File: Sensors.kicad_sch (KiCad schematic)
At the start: 10 parts, among them U11 LSM6DSO32, U12 LIS2MDL, U13 MS5611-01BA

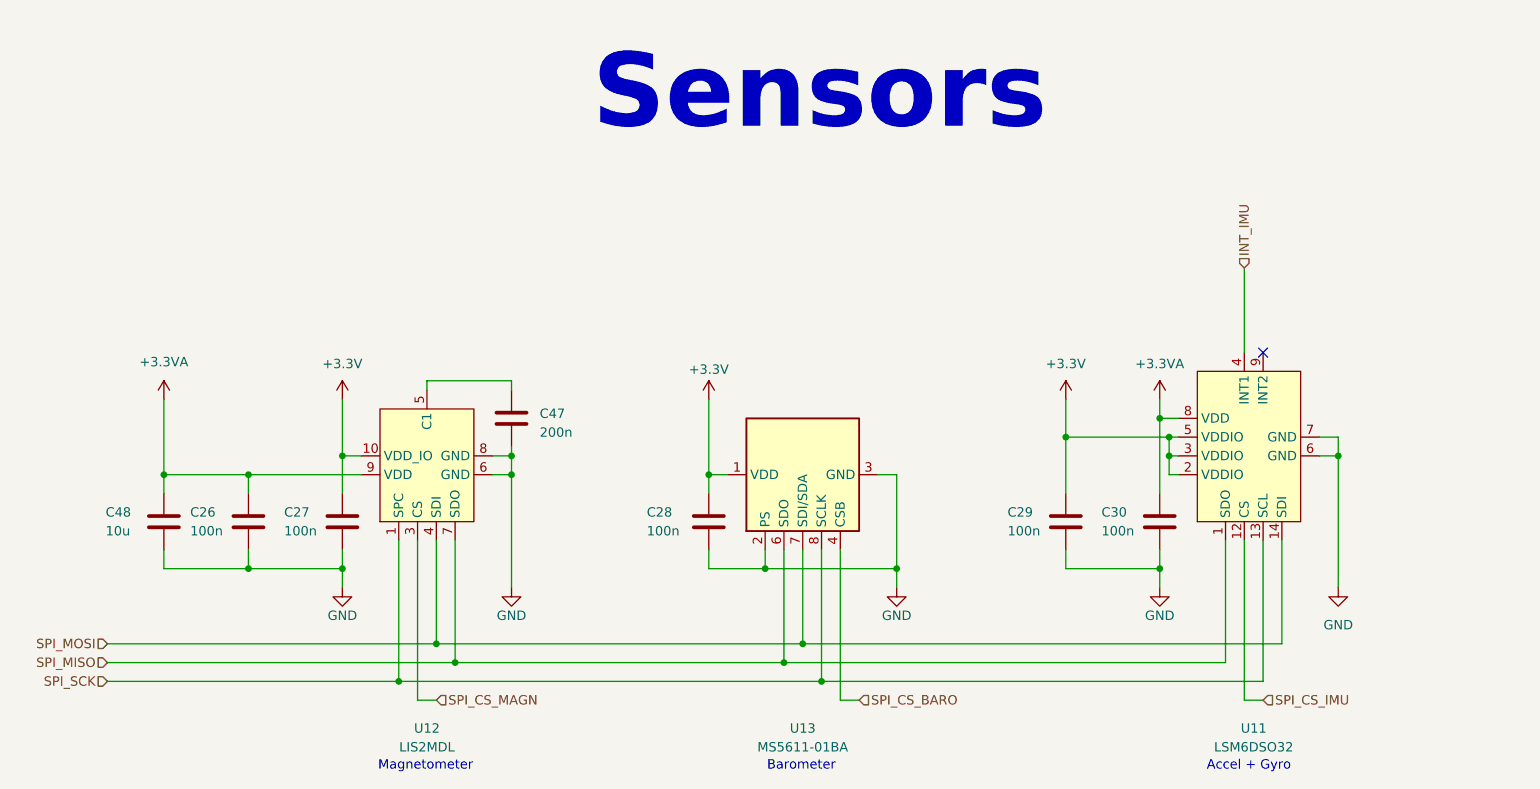
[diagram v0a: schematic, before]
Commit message: :building_construction: Simplify power circuit and consolidate BOM
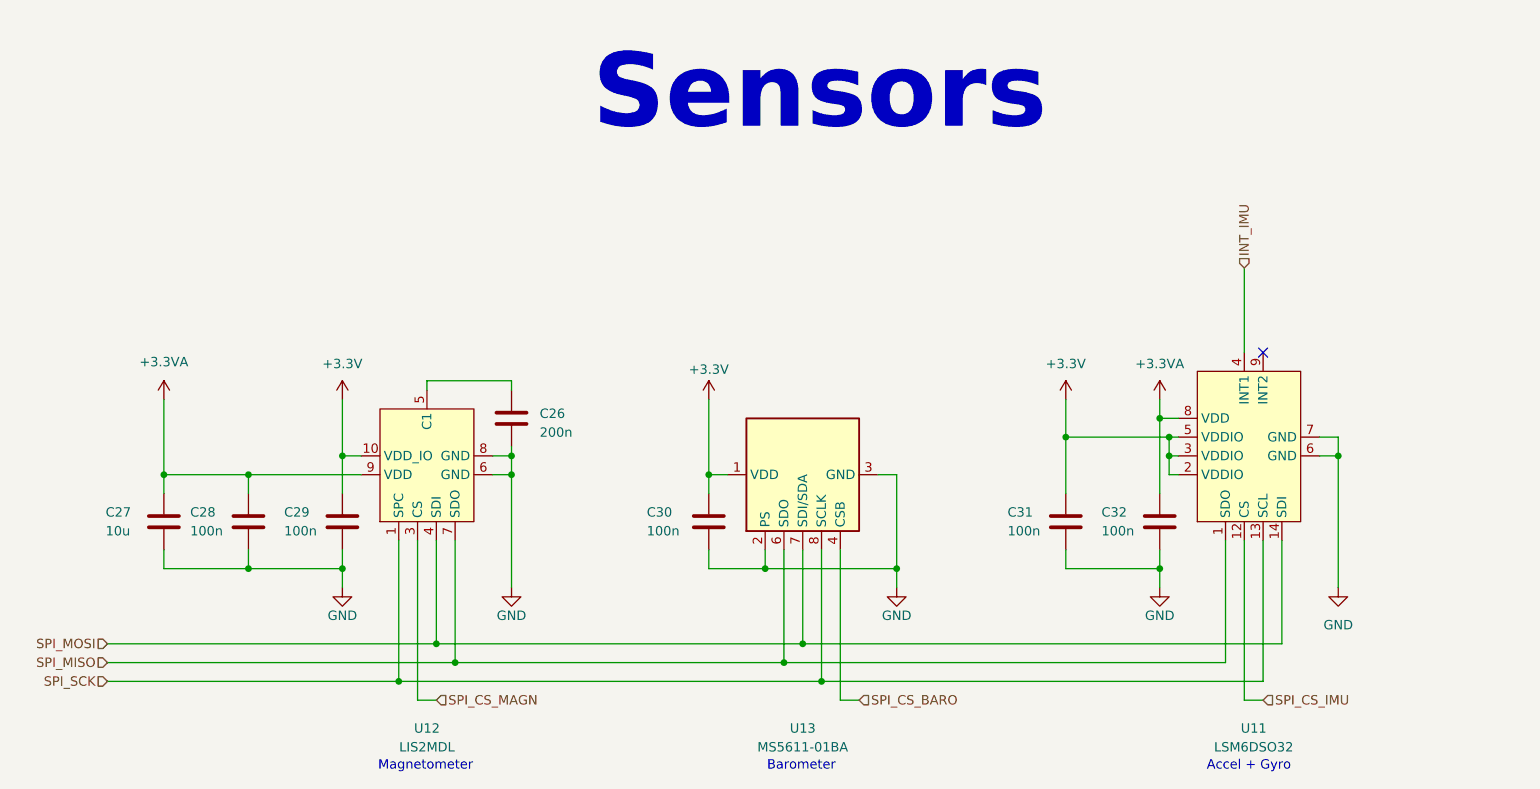
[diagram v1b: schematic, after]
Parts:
- renumbered C47 to C26, C48 to C27, C26 to C28, C27 to C29, C28 to C30, C29 to C31, C30 to C32
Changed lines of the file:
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@@
   (symbol (lib_id "Device:C") (at 58.42 102.87 0) (unit 1)
     (in_bom yes) (on_board yes) (dnp no)
-    (property "Reference" "C48" (at 50.546 101.6 0)
+    (property "Reference" "C27" (at 50.546 101.6 0)
       (effects (font (size 1.27 1.27)) (justify left))
     )
@@
   (symbol (lib_id "power:GND") (at 105.41 111.76 0) (unit 1)
     (in_bom yes) (on_board yes) (dnp no)
-    (property "Reference" "#PWR051" (at 105.41 118.11 0)
+    (property "Reference" "#PWR052" (at 105.41 118.11 0)
       (effects (font (size 1.27 1.27)) hide)
     )
@@
       (project "Nova"
         (path "/0c006d9f-ae30-49aa-ab15-ff0bec4de0e8/b4564e06-ae37-4733-9020-dc4bb7ce2d2c"
-          (reference "#PWR051") (unit 1)
+          (reference "#PWR052") (unit 1)
         )
       )
@@
   (symbol (lib_id "power:GND") (at 193.04 111.76 0) (unit 1)
     (in_bom yes) (on_board yes) (dnp no)
-    (property "Reference" "#PWR053" (at 193.04 118.11 0)
+    (property "Reference" "#PWR054" (at 193.04 118.11 0)
       (effects (font (size 1.27 1.27)) hide)
     )
@@
       (project "Nova"
         (path "/0c006d9f-ae30-49aa-ab15-ff0bec4de0e8/b4564e06-ae37-4733-9020-dc4bb7ce2d2c"
-          (reference "#PWR053") (unit 1)
+          (reference "#PWR054") (unit 1)
         )
       )
@@
   (symbol (lib_id "Device:C") (at 193.04 102.87 0) (unit 1)
     (in_bom yes) (on_board yes) (dnp no)
-    (property "Reference" "C30" (at 185.166 101.6 0)
+    (property "Reference" "C32" (at 185.166 101.6 0)
       (effects (font (size 1.27 1.27)) (justify left))
     )
@@
   (symbol (lib_id "Device:C") (at 105.41 88.9 0) (unit 1)
     (in_bom yes) (on_board yes) (dnp no) (fields_autoplaced)
-    (property "Reference" "C47" (at 109.22 88.265 0)
+    (property "Reference" "C26" (at 109.22 88.265 0)
       (effects (font (size 1.27 1.27)) (justify left))
     )
@@
   (symbol (lib_id "power:+3.3VA") (at 193.04 86.36 0) (unit 1)
     (in_bom yes) (on_board yes) (dnp no)
-    (property "Reference" "#PWR049" (at 193.04 90.17 0)
+    (property "Reference" "#PWR050" (at 193.04 90.17 0)
       (effects (font (size 1.27 1.27)) hide)
     )
@@
       (project "Nova"
         (path "/0c006d9f-ae30-49aa-ab15-ff0bec4de0e8/b4564e06-ae37-4733-9020-dc4bb7ce2d2c"
-          (reference "#PWR049") (unit 1)
+          (reference "#PWR050") (unit 1)
         )
       )
@@
   (symbol (lib_id "Device:C") (at 69.85 102.87 0) (unit 1)
     (in_bom yes) (on_board yes) (dnp no)
-    (property "Reference" "C26" (at 61.976 101.6 0)
+    (property "Reference" "C28" (at 61.976 101.6 0)
       (effects (font (size 1.27 1.27)) (justify left))
     )
@@
   (symbol (lib_id "Device:C") (at 82.55 102.87 0) (unit 1)
     (in_bom yes) (on_board yes) (dnp no)
-    (property "Reference" "C27" (at 74.676 101.6 0)
+    (property "Reference" "C29" (at 74.676 101.6 0)
       (effects (font (size 1.27 1.27)) (justify left))
     )
@@
   (symbol (lib_id "Device:C") (at 180.34 102.87 0) (unit 1)
     (in_bom yes) (on_board yes) (dnp no)
-    (property "Reference" "C29" (at 172.466 101.6 0)
+    (property "Reference" "C31" (at 172.466 101.6 0)
       (effects (font (size 1.27 1.27)) (justify left))
     )
@@
   (symbol (lib_id "Device:C") (at 132.08 102.87 0) (unit 1)
     (in_bom yes) (on_board yes) (dnp no)
-    (property "Reference" "C28" (at 123.698 101.6 0)
+    (property "Reference" "C30" (at 123.698 101.6 0)
       (effects (font (size 1.27 1.27)) (justify left))
     )
@@
   (symbol (lib_id "power:+3.3V") (at 82.55 86.36 0) (unit 1)
     (in_bom yes) (on_board yes) (dnp no) (fields_autoplaced)
-    (property "Reference" "#PWR045" (at 82.55 90.17 0)
+    (property "Reference" "#PWR047" (at 82.55 90.17 0)
       (effects (font (size 1.27 1.27)) hide)
     )
@@
       (project "Nova"
         (path "/0c006d9f-ae30-49aa-ab15-ff0bec4de0e8/b4564e06-ae37-4733-9020-dc4bb7ce2d2c"
-          (reference "#PWR046") (unit 1)
+          (reference "#PWR047") (unit 1)
         )
       )
@@
   (symbol (lib_id "power:+3.3V") (at 180.34 86.36 0) (unit 1)
     (in_bom yes) (on_board yes) (dnp no) (fields_autoplaced)
-    (property "Reference" "#PWR048" (at 180.34 90.17 0)
+    (property "Reference" "#PWR049" (at 180.34 90.17 0)
       (effects (font (size 1.27 1.27)) hide)
     )
@@
       (project "Nova"
         (path "/0c006d9f-ae30-49aa-ab15-ff0bec4de0e8/b4564e06-ae37-4733-9020-dc4bb7ce2d2c"
-          (reference "#PWR048") (unit 1)
+          (reference "#PWR049") (unit 1)
         )
       )
@@
   (symbol (lib_id "power:GND") (at 157.48 111.76 0) (unit 1)
     (in_bom yes) (on_board yes) (dnp no)
-    (property "Reference" "#PWR052" (at 157.48 118.11 0)
+    (property "Reference" "#PWR053" (at 157.48 118.11 0)
       (effects (font (size 1.27 1.27)) hide)
     )
@@
       (project "Nova"
         (path "/0c006d9f-ae30-49aa-ab15-ff0bec4de0e8/b4564e06-ae37-4733-9020-dc4bb7ce2d2c"
-          (reference "#PWR052") (unit 1)
+          (reference "#PWR053") (unit 1)
         )
       )
@@
   (symbol (lib_id "power:GND") (at 217.17 111.76 0) (unit 1)
     (in_bom yes) (on_board yes) (dnp no) (fields_autoplaced)
-    (property "Reference" "#PWR054" (at 217.17 118.11 0)
+    (property "Reference" "#PWR055" (at 217.17 118.11 0)
       (effects (font (size 1.27 1.27)) hide)
     )
@@
       (project "Nova"
         (path "/0c006d9f-ae30-49aa-ab15-ff0bec4de0e8/b4564e06-ae37-4733-9020-dc4bb7ce2d2c"
-          (reference "#PWR054") (unit 1)
+          (reference "#PWR055") (unit 1)
         )
       )
@@
   (symbol (lib_id "power:+3.3V") (at 132.08 86.36 0) (unit 1)
     (in_bom yes) (on_board yes) (dnp no)
-    (property "Reference" "#PWR047" (at 132.08 90.17 0)
+    (property "Reference" "#PWR048" (at 132.08 90.17 0)
       (effects (font (size 1.27 1.27)) hide)
     )
@@
       (project "Nova"
         (path "/0c006d9f-ae30-49aa-ab15-ff0bec4de0e8/b4564e06-ae37-4733-9020-dc4bb7ce2d2c"
-          (reference "#PWR047") (unit 1)
+          (reference "#PWR048") (unit 1)
         )
       )
@@
   (symbol (lib_id "power:GND") (at 82.55 111.76 0) (unit 1)
     (in_bom yes) (on_board yes) (dnp no)
-    (property "Reference" "#PWR050" (at 82.55 118.11 0)
+    (property "Reference" "#PWR051" (at 82.55 118.11 0)
       (effects (font (size 1.27 1.27)) hide)
     )
@@
       (project "Nova"
         (path "/0c006d9f-ae30-49aa-ab15-ff0bec4de0e8/b4564e06-ae37-4733-9020-dc4bb7ce2d2c"
-          (reference "#PWR050") (unit 1)
+          (reference "#PWR051") (unit 1)
         )
       )
@@
       (project "Nova"
         (path "/0c006d9f-ae30-49aa-ab15-ff0bec4de0e8/b4564e06-ae37-4733-9020-dc4bb7ce2d2c"
-          (reference "#PWR045") (unit 1)
-        )
-      )
+          (reference "#PWR046") (unit 1)
+        )
+      )

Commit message: :building_construction: Replace debug header with TagConnect and inline STM32 decoupling caps
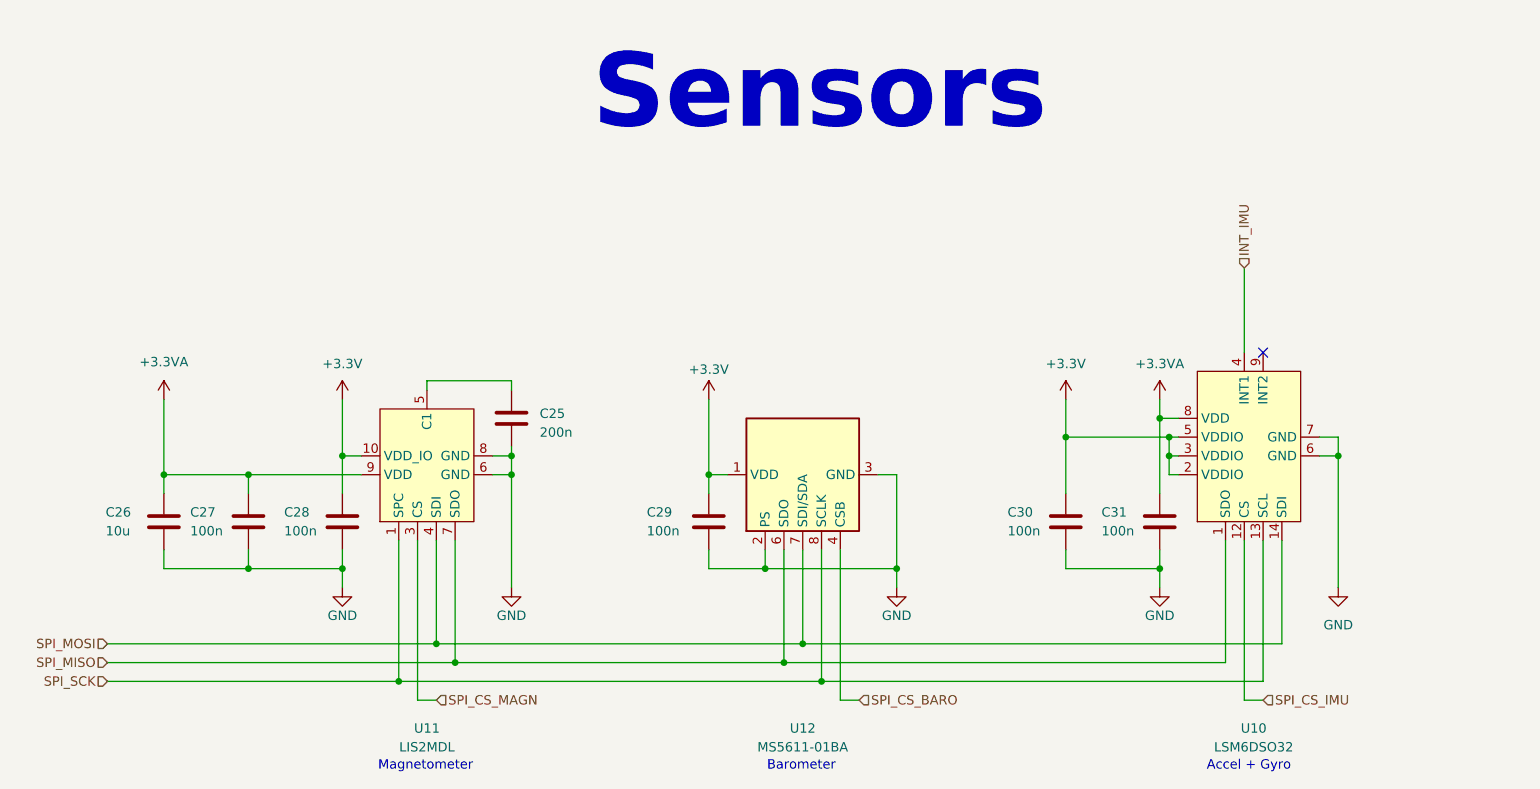
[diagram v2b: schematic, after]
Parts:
- renumbered C26 to C25, C27 to C26, C28 to C27, C29 to C28, C30 to C29, C31 to C30, C32 to C31, U11 to U10, U12 to U11, U13 to U12
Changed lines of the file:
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@@
   (symbol (lib_id "Device:C") (at 58.42 102.87 0) (unit 1)
     (in_bom yes) (on_board yes) (dnp no)
-    (property "Reference" "C27" (at 50.546 101.6 0)
+    (property "Reference" "C26" (at 50.546 101.6 0)
       (effects (font (size 1.27 1.27)) (justify left))
     )
@@
       (project "Nova"
         (path "/0c006d9f-ae30-49aa-ab15-ff0bec4de0e8/b4564e06-ae37-4733-9020-dc4bb7ce2d2c"
-          (reference "C27") (unit 1)
+          (reference "C26") (unit 1)
         )
       )
@@
   (symbol (lib_id "Odyssey:LIS2MDL") (at 87.63 95.25 90) (unit 1)
     (in_bom yes) (on_board yes) (dnp no)
-    (property "Reference" "U12" (at 93.98 130.81 90)
+    (property "Reference" "U11" (at 93.98 130.81 90)
       (effects (font (size 1.27 1.27)))
     )
@@
       (project "Nova"
         (path "/0c006d9f-ae30-49aa-ab15-ff0bec4de0e8/b4564e06-ae37-4733-9020-dc4bb7ce2d2c"
-          (reference "U12") (unit 1)
+          (reference "U11") (unit 1)
         )
       )
@@
   (symbol (lib_id "Device:C") (at 193.04 102.87 0) (unit 1)
     (in_bom yes) (on_board yes) (dnp no)
-    (property "Reference" "C32" (at 185.166 101.6 0)
+    (property "Reference" "C31" (at 185.166 101.6 0)
       (effects (font (size 1.27 1.27)) (justify left))
     )
@@
       (project "Nova"
         (path "/0c006d9f-ae30-49aa-ab15-ff0bec4de0e8/b4564e06-ae37-4733-9020-dc4bb7ce2d2c"
-          (reference "C32") (unit 1)
+          (reference "C31") (unit 1)
         )
       )
@@
   (symbol (lib_id "Device:C") (at 105.41 88.9 0) (unit 1)
     (in_bom yes) (on_board yes) (dnp no) (fields_autoplaced)
-    (property "Reference" "C26" (at 109.22 88.265 0)
+    (property "Reference" "C25" (at 109.22 88.265 0)
       (effects (font (size 1.27 1.27)) (justify left))
     )
@@
       (project "Nova"
         (path "/0c006d9f-ae30-49aa-ab15-ff0bec4de0e8/b4564e06-ae37-4733-9020-dc4bb7ce2d2c"
-          (reference "C26") (unit 1)
+          (reference "C25") (unit 1)
         )
       )
@@
   (symbol (lib_id "Device:C") (at 69.85 102.87 0) (unit 1)
     (in_bom yes) (on_board yes) (dnp no)
-    (property "Reference" "C28" (at 61.976 101.6 0)
+    (property "Reference" "C27" (at 61.976 101.6 0)
       (effects (font (size 1.27 1.27)) (justify left))
     )
@@
       (project "Nova"
         (path "/0c006d9f-ae30-49aa-ab15-ff0bec4de0e8/b4564e06-ae37-4733-9020-dc4bb7ce2d2c"
+          (reference "C27") (unit 1)
+        )
+      )
+    )
+  )
+  (symbol (lib_id "Device:C") (at 82.55 102.87 0) (unit 1)
+    (in_bom yes) (on_board yes) (dnp no)
+    (property "Reference" "C28" (at 74.676 101.6 0)
+      (effects (font (size 1.27 1.27)) (justify left))
+    )
+    (property "Value" "100n" (at 74.676 104.14 0)
+      (effects (font (size 1.27 1.27)) (justify left))
+    )
+    (property "Footprint" "Capacitor_SMD:C_0402_1005Metric_Pad0.74x0.62mm_HandSolder" (at 83.5152 106.68 0)
+      (effects (font (size 1.27 1.27)) hide)
+    )
+    (property "Datasheet" "~" (at 82.55 102.87 0)
+      (effects (font (size 1.27 1.27)) hide)
+    )
+    (pin "1")
+    (pin "2")
+    (instances
+      (project "Nova"
+        (path "/0c006d9f-ae30-49aa-ab15-ff0bec4de0e8/b4564e06-ae37-4733-9020-dc4bb7ce2d2c"
           (reference "C28") (unit 1)
         )
@@
     )
   )
-  (symbol (lib_id "Device:C") (at 82.55 102.87 0) (unit 1)
-    (in_bom yes) (on_board yes) (dnp no)
-    (property "Reference" "C29" (at 74.676 101.6 0)
-      (effects (font (size 1.27 1.27)) (justify left))
-    )
-    (property "Value" "100n" (at 74.676 104.14 0)
-      (effects (font (size 1.27 1.27)) (justify left))
-    )
-    (property "Footprint" "Capacitor_SMD:C_0402_1005Metric_Pad0.74x0.62mm_HandSolder" (at 83.5152 106.68 0)
-      (effects (font (size 1.27 1.27)) hide)
-    )
-    (property "Datasheet" "~" (at 82.55 102.87 0)
+  (symbol (lib_id "Device:C") (at 180.34 102.87 0) (unit 1)
+    (in_bom yes) (on_board yes) (dnp no)
+    (property "Reference" "C30" (at 172.466 101.6 0)
+      (effects (font (size 1.27 1.27)) (justify left))
+    )
+    (property "Value" "100n" (at 172.466 104.14 0)
+      (effects (font (size 1.27 1.27)) (justify left))
+    )
+    (property "Footprint" "Capacitor_SMD:C_0402_1005Metric_Pad0.74x0.62mm_HandSolder" (at 181.3052 106.68 0)
+      (effects (font (size 1.27 1.27)) hide)
+    )
+    (property "Datasheet" "~" (at 180.34 102.87 0)
+      (effects (font (size 1.27 1.27)) hide)
+    )
+    (pin "1")
+    (pin "2")
+    (instances
+      (project "Nova"
+        (path "/0c006d9f-ae30-49aa-ab15-ff0bec4de0e8/b4564e06-ae37-4733-9020-dc4bb7ce2d2c"
+          (reference "C30") (unit 1)
+        )
+      )
+    )
+  )
+  (symbol (lib_id "Device:C") (at 132.08 102.87 0) (unit 1)
+    (in_bom yes) (on_board yes) (dnp no)
+    (property "Reference" "C29" (at 123.698 101.6 0)
+      (effects (font (size 1.27 1.27)) (justify left))
+    )
+    (property "Value" "100n" (at 123.698 104.14 0)
+      (effects (font (size 1.27 1.27)) (justify left))
+    )
+    (property "Footprint" "Capacitor_SMD:C_0402_1005Metric_Pad0.74x0.62mm_HandSolder" (at 133.0452 106.68 0)
+      (effects (font (size 1.27 1.27)) hide)
+    )
+    (property "Datasheet" "~" (at 132.08 102.87 0)
       (effects (font (size 1.27 1.27)) hide)
     )
@@
         (path "/0c006d9f-ae30-49aa-ab15-ff0bec4de0e8/b4564e06-ae37-4733-9020-dc4bb7ce2d2c"
           (reference "C29") (unit 1)
-        )
-      )
-    )
-  )
-  (symbol (lib_id "Device:C") (at 180.34 102.87 0) (unit 1)
-    (in_bom yes) (on_board yes) (dnp no)
-    (property "Reference" "C31" (at 172.466 101.6 0)
-      (effects (font (size 1.27 1.27)) (justify left))
-    )
-    (property "Value" "100n" (at 172.466 104.14 0)
-      (effects (font (size 1.27 1.27)) (justify left))
-    )
-    (property "Footprint" "Capacitor_SMD:C_0402_1005Metric_Pad0.74x0.62mm_HandSolder" (at 181.3052 106.68 0)
-      (effects (font (size 1.27 1.27)) hide)
-    )
-    (property "Datasheet" "~" (at 180.34 102.87 0)
-      (effects (font (size 1.27 1.27)) hide)
-    )
-    (pin "1")
-    (pin "2")
-    (instances
-      (project "Nova"
-        (path "/0c006d9f-ae30-49aa-ab15-ff0bec4de0e8/b4564e06-ae37-4733-9020-dc4bb7ce2d2c"
-          (reference "C31") (unit 1)
-        )
-      )
-    )
-  )
-  (symbol (lib_id "Device:C") (at 132.08 102.87 0) (unit 1)
-    (in_bom yes) (on_board yes) (dnp no)
-    (property "Reference" "C30" (at 123.698 101.6 0)
-      (effects (font (size 1.27 1.27)) (justify left))
-    )
-    (property "Value" "100n" (at 123.698 104.14 0)
-      (effects (font (size 1.27 1.27)) (justify left))
-    )
-    (property "Footprint" "Capacitor_SMD:C_0402_1005Metric_Pad0.74x0.62mm_HandSolder" (at 133.0452 106.68 0)
-      (effects (font (size 1.27 1.27)) hide)
-    )
-    (property "Datasheet" "~" (at 132.08 102.87 0)
-      (effects (font (size 1.27 1.27)) hide)
-    )
-    (pin "1")
-    (pin "2")
-    (instances
-      (project "Nova"
-        (path "/0c006d9f-ae30-49aa-ab15-ff0bec4de0e8/b4564e06-ae37-4733-9020-dc4bb7ce2d2c"
-          (reference "C30") (unit 1)
         )
       )
@@
   (symbol (lib_id "Sensor_Pressure:MS5611-01BA") (at 144.78 96.52 90) (unit 1)
     (in_bom yes) (on_board yes) (dnp no)
-    (property "Reference" "U13" (at 144.78 130.81 90)
+    (property "Reference" "U12" (at 144.78 130.81 90)
       (effects (font (size 1.27 1.27)))
     )
@@
       (project "Nova"
         (path "/0c006d9f-ae30-49aa-ab15-ff0bec4de0e8/b4564e06-ae37-4733-9020-dc4bb7ce2d2c"
-          (reference "U13") (unit 1)
+          (reference "U12") (unit 1)
         )
       )
@@
   (symbol (lib_id "Odyssey:LSM6DSO32") (at 198.12 92.71 90) (unit 1)
     (in_bom yes) (on_board yes) (dnp no)
-    (property "Reference" "U11" (at 205.74 130.81 90)
+    (property "Reference" "U10" (at 205.74 130.81 90)
       (effects (font (size 1.27 1.27)))
     )
@@
       (project "Nova"
         (path "/0c006d9f-ae30-49aa-ab15-ff0bec4de0e8/b4564e06-ae37-4733-9020-dc4bb7ce2d2c"
-          (reference "U11") (unit 1)
-        )
-      )
+          (reference "U10") (unit 1)
+        )
+      )
